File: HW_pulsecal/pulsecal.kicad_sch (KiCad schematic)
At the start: 35 parts, among them J1 BNC_CONN, Q3 FDG6301N, U1 TLV9061IDBVR, U2 TLV9061IDBVR, U5 STM32G030C8Tx

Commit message: update
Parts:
- added C25: 104/50V, Capacitor_SMD:C_0402_1005Metric, symbol Device:C
- added FB1: 600R/100M, Inductor_SMD:L_0603_1608Metric, symbol Device:FerriteBead_Small
- added J4: Conn_01x04, Connector_PinSocket_2.54mm:PinSocket_1x04_P2.54mm_Vertical, symbol Connector_Generic:Conn_01x04
- C20, C21: value 101/50 -> 101/50V
- C7: value 106/6.3V -> 106/16V; footprint Capacitor_SMD:C_0402_1005Metric -> Capacitor_SMD:C_0603_1608Metric
- J1: footprint (none) -> NewLib:BNC_3pin
- R1: footprint Resistor_SMD:R_0402_1005Metric -> Resistor_SMD:R_0603_1608Metric
- R12, R13: value 500M -> 1G
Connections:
- net +3V3: now also FB1.1, J4.1 (Pin_1); no longer U5.5 (VREF+)
- net GND: now also C25.1, J4.3 (Pin_3)
- net HV_ADC: now also U5.12 (PA1); no longer U5.11 (PA0)
- net SWCLK: now also J4.4 (Pin_4)
- net SWDIO: now also J4.2 (Pin_2)
- net dac_fb: now also U5.13 (PA2); no longer U5.12 (PA1)
- net at R10.2, R6.1, U2.1: now also R14.1
- net at R6.2, U2.4 (-): no longer R14.1
- net key_output: now reaches U5.1 (PC13)
- net key_pulse: now reaches U5.2 (PC14)
- net key_add: now reaches U5.3 (PC15)
- net key_sub: now reaches U5.45 (PB6)
- net key_volt: now reaches U5.46 (PB7)
- net key_move: now reaches U5.47 (PB8)
- net key_freq: now reaches U5.48 (PB9)
- new net VAA: C25.2, FB1.2, U5.5 (VREF+)
- new net bat_adc: U5.11 (PA0)
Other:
- note added: "35"
- moved on the sheet: C23, C24, R14

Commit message: update
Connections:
- net DISP_A: now also U5.30 (PC6)
- net DISP_B: now also U5.34 (PA12/PA10)
- net DISP_C: now also U5.23 (PB11)
- net DISP_D: now also U5.21 (PB2)
- net DISP_DIG1: now also U5.27 (PB15)
- net DISP_DIG2: now also U5.22 (PB10)
- net DISP_DIG3: now also U5.32 (PA10/NC)
- net DISP_DIG4: now also U5.38 (PD0)
- net DISP_DIG5: now also U5.40 (PD2)
- net DISP_DIG6: now also U5.44 (PB5)
- net DISP_DP: now also U5.29 (PA9/NC)
- net DISP_E: now also U5.31 (PC7)
- net DISP_F: now also U5.20 (PB1)
- net DISP_G1: now also U5.43 (PB4)
- net DISP_G2: now also U5.41 (PD3)
- net DISP_H: now also U5.26 (PB14)
- net DISP_J: now also U5.24 (PB12)
- net DISP_K: now also U5.42 (PB3)
- net DISP_L: now also U5.39 (PD1)
- net DISP_M: now also U5.37 (PA15)
- net DISP_N: now also U5.33 (PA11/PA9)
- no-connect marks 0 -> 6
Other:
- moved on the sheet: J4

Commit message: update
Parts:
- R1, R15: value 1k -> 1K
- R11: value 2.2k -> 2.2K
- R12, R13: value 1G -> 500M
- R14, R5, R6, R7: value 10k -> 10K
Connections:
- no-connect marks 6 -> 7
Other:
- moved on the sheet: C20, C21, J4, R8, R9

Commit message: Update pulsecal.kicad_sch
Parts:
- R15: value 1K -> NC
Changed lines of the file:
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@@
 			)
 		)
-		(property "Value" "1K"
+		(property "Value" "NC"
 			(at 156.21 73.914 90)
 			(effects

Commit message: update
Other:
- note added: "建议用一颗5~10nF的高压电容代替"
- company: (none) -> 模拟龙仪器仪表
- title: (none) -> 率表/定标器测试工具
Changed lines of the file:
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@@
 	(generator_version "8.0")
 	(paper "A4")
+	(title_block
+		(title "率表/定标器测试工具")
+		(date "2025-06-14")
+		(rev "V1.1")
+		(company "模拟龙仪器仪表")
+	)
 	(junction
 		(at 118.11 116.84)
@@
 	)
 	(rectangle
+		(start 40.64 97.79)
+		(end 63.5 116.84)
+		(stroke
+			(width 0)
+			(type default)
+		)
+		(fill
+			(type none)
+		)
+	)
+	(rectangle
 		(start 91.44 99.06)
 		(end 102.87 106.68)
@@
 		)
 	)
+	(text "建议用一颗5~10nF的高压电容代替"
+		(exclude_from_sim no)
+		(at 52.324 96.52 0)
+		(effects
+			(font
+				(size 1.27 1.27)
+			)
+		)
+	)
 	(text "CH1N\n\nCH1"
 		(exclude_from_sim no)
@@
 	)
 	(sheet
-		(at 180.34 170.18)
-		(size 12.7 8.89)
-		(fields_autoplaced yes)
+		(at 180.34 168.91)
+		(size 12.7 6.35)
 		(stroke
 			(width 0.1524)
@@
 		)
 		(property "Sheetname" "POWER"
-			(at 180.34 169.4684 0)
+			(at 183.388 172.72 0)
 			(effects
 				(font
@@
 		)
 		(property "Sheetfile" "power.kicad_sch"
-			(at 180.34 179.6546 0)
+			(at 180.34 175.8446 0)
 			(effects
 				(font
@@
 	)
 	(sheet
-		(at 195.58 170.18)
-		(size 12.7 8.89)
-		(fields_autoplaced yes)
+		(at 195.58 168.91)
+		(size 12.7 6.35)
 		(stroke
 			(width 0.1524)
@@
 		)
 		(property "Sheetname" "DISP"
-			(at 195.58 169.4684 0)
+			(at 198.628 172.72 0)
 			(effects
 				(font
@@
 		)
 		(property "Sheetfile" "disp.kicad_sch"
-			(at 195.58 179.6546 0)
+			(at 195.58 175.8446 0)
 			(effects
 				(font

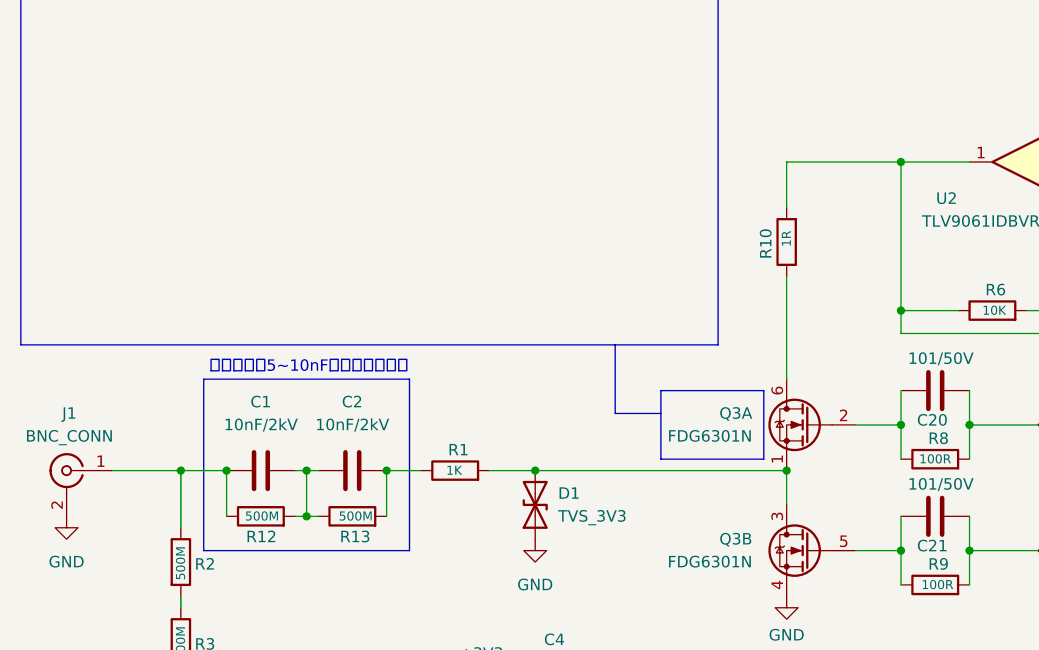
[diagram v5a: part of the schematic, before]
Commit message: 更新
增加了一个电阻，可以极大的减少低压输出的振铃
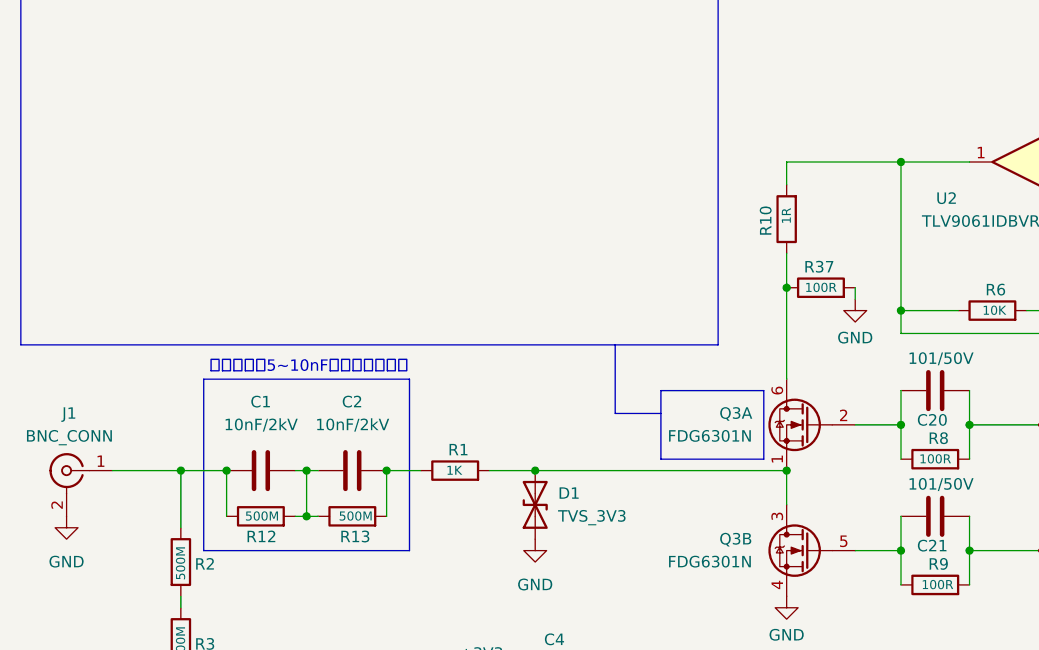
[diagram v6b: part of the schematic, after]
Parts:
- added R37: 100R, Resistor_SMD:R_0402_1005Metric, symbol Device:R
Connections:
- net GND: now also R37.2
- net at Q3.6 (D), R10.1: now also R37.1
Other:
- moved on the sheet: R10
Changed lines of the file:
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@@
 (kicad_sch
-	(version 20231120)
+	(version 20250114)
 	(generator "eeschema")
-	(generator_version "8.0")
+	(generator_version "9.0")
 	(paper "A4")
 	(title_block
@@
 		(company "模拟龙仪器仪表")
 	)
+	(rectangle
+		(start 213.36 16.51)
+		(end 281.94 158.75)
+		(stroke
+			(width 0)
+			(type default)
+		)
+		(fill
+			(type none)
+		)
+	)
+	(rectangle
+		(start 20.32 16.51)
+		(end 97.79 93.98)
+		(stroke
+			(width 0)
+			(type default)
+		)
+		(fill
+			(type none)
+		)
+	)
+	(rectangle
+		(start 40.64 97.79)
+		(end 63.5 116.84)
+		(stroke
+			(width 0)
+			(type default)
+		)
+		(fill
+			(type none)
+		)
+	)
+	(rectangle
+		(start 91.44 99.06)
+		(end 102.87 106.68)
+		(stroke
+			(width 0)
+			(type default)
+		)
+		(fill
+			(type none)
+		)
+	)
+	(text "0.6uA max"
+		(exclude_from_sim no)
+		(at 60.452 136.144 0)
+		(effects
+			(font
+				(size 1.27 1.27)
+			)
+		)
+	)
+	(text "35"
+		(exclude_from_sim no)
+		(at 275.082 154.94 0)
+		(effects
+			(font
+				(size 1.27 1.27)
+			)
+		)
+	)
+	(text "建议用一颗5~10nF的高压电容代替"
+		(exclude_from_sim no)
+		(at 52.324 96.52 0)
+		(effects
+			(font
+				(size 1.27 1.27)
+			)
+		)
+	)
+	(text "CH1N\n\nCH1"
+		(exclude_from_sim no)
+		(at 157.48 40.386 0)
+		(effects
+			(font
+				(size 1.27 1.27)
+				(color 255 255 255 1)
+			)
+		)
+	)
+	(text "1000:1"
+		(exclude_from_sim no)
+		(at 42.672 132.334 0)
+		(effects
+			(font
+				(size 1.27 1.27)
+			)
+		)
+	)
 	(junction
 		(at 118.11 116.84)
@@
 	)
 	(junction
+		(at 105.41 87.63)
+		(diameter 0)
+		(color 0 0 0 0)
+	)
+	(junction
 		(at 38.1 107.95)
 		(diameter 0)
@@
 	(wire
 		(pts
+			(xy 113.03 88.9) (xy 113.03 87.63)
+		)
+		(stroke
+			(width 0)
+			(type default)
+		)
+	)
+	(wire
+		(pts
 			(xy 72.39 107.95) (xy 77.47 107.95)
 		)
@@
 	(wire
 		(pts
+			(xy 105.41 87.63) (xy 105.41 97.79)
+		)
+		(stroke
+			(width 0)
+			(type default)
+		)
+	)
+	(wire
+		(pts
 			(xy 118.11 90.17) (xy 118.11 92.71)
 		)
@@
 	(wire
 		(pts
-			(xy 105.41 86.36) (xy 105.41 97.79)
+			(xy 105.41 83.82) (xy 105.41 87.63)
 		)
 		(stroke
@@
 	(wire
 		(pts
-			(xy 105.41 73.66) (xy 105.41 78.74)
+			(xy 105.41 73.66) (xy 105.41 76.2)
 		)
 		(stroke
@@
 		)
 	)
-	(rectangle
-		(start 213.36 16.51)
-		(end 281.94 158.75)
-		(stroke
-			(width 0)
-			(type default)
-		)
-		(fill
-			(type none)
-		)
-	)
-	(rectangle
-		(start 20.32 16.51)
-		(end 97.79 93.98)
-		(stroke
-			(width 0)
-			(type default)
-		)
-		(fill
-			(type none)
-		)
-	)
-	(rectangle
-		(start 40.64 97.79)
-		(end 63.5 116.84)
-		(stroke
-			(width 0)
-			(type default)
-		)
-		(fill
-			(type none)
-		)
-	)
-	(rectangle
-		(start 91.44 99.06)
-		(end 102.87 106.68)
-		(stroke
-			(width 0)
-			(type default)
-		)
-		(fill
-			(type none)
-		)
-	)
 	(image
 		(at 157.48 34.29)
@@
 		)
 	)
-	(text "0.6uA max"
-		(exclude_from_sim no)
-		(at 60.452 136.144 0)
-		(effects
-			(font
-				(size 1.27 1.27)
-			)
-		)
-	)
-	(text "35"
-		(exclude_from_sim no)
-		(at 275.082 154.94 0)
-		(effects
-			(font
-				(size 1.27 1.27)
-			)
-		)
-	)
-	(text "建议用一颗5~10nF的高压电容代替"
-		(exclude_from_sim no)
-		(at 52.324 96.52 0)
-		(effects
-			(font
-				(size 1.27 1.27)
-			)
-		)
-	)
-	(text "CH1N\n\nCH1"
-		(exclude_from_sim no)
-		(at 157.48 40.386 0)
-		(effects
-			(font
-				(size 1.27 1.27)
-				(color 255 255 255 1)
-			)
-		)
-	)
-	(text "1000:1"
-		(exclude_from_sim no)
-		(at 42.672 132.334 0)
-		(effects
-			(font
-				(size 1.27 1.27)
-			)
-		)
-	)
 	(label "dac"
 		(at 167.64 71.12 0)
-		(fields_autoplaced yes)
 		(effects
 			(font
@@
 	)
 	(symbol
+		(lib_id "Device:R")
+		(at 109.22 87.63 90)
+		(unit 1)
+		(exclude_from_sim no)
+		(in_bom yes)
+		(on_board yes)
+		(dnp no)
+		(property "Reference" "R37"
+			(at 110.744 85.344 90)
+			(effects
+				(font
+					(size 1.27 1.27)
+				)
+				(justify left)
+			)
+		)
+		(property "Value" "100R"
+			(at 110.998 87.63 90)
+			(effects
+				(font
+					(size 1 1)
+				)
+				(justify left)
+			)
+		)
+		(property "Footprint" "Resistor_SMD:R_0402_1005Metric"
+			(at 109.22 89.408 90)
+			(effects
+				(font
+					(size 1.27 1.27)
+				)
+				(hide yes)
+			)
+		)
+		(property "Datasheet" "~"
+			(at 109.22 87.63 0)
+			(effects
+				(font
+					(size 1.27 1.27)
+				)
+				(hide yes)
+			)
+		)
+		(property "Description" "Resistor"
+			(at 109.22 87.63 0)
+			(effects
+				(font
+					(size 1.27 1.27)
+				)
+				(hide yes)
+			)
+		)
+		(pin "2"
+		)
+		(pin "1"
+		)
+		(instances
+			(project "pulsecal"
+				(path "/43467254-5f0e-4dea-8ff8-85167d0157c0"
+					(reference "R37")
+					(unit 1)
+				)
+			)
+		)
+	)
+	(symbol
 		(lib_id "Device:C")
 		(at 76.2 132.08 90)
@@
 	)
 	(symbol
+		(lib_id "power:GND")
+		(at 113.03 88.9 0)
+		(mirror y)
+		(unit 1)
+		(exclude_from_sim no)
+		(in_bom yes)
+		(on_board yes)
+		(dnp no)
+		(property "Reference" "#PWR071"
+			(at 113.03 95.25 0)
+			(effects
+				(font
+					(size 1.27 1.27)
+				)
+				(hide yes)
+			)
+		)
+		(property "Value" "GND"
+			(at 113.03 93.218 0)
+			(effects
+				(font
+					(size 1.27 1.27)
+				)
+			)
+		)
+		(property "Footprint" ""
+			(at 113.03 88.9 0)
+			(effects
+				(font
+					(size 1.27 1.27)
+				)
+				(hide yes)
+			)
+		)
+		(property "Datasheet" ""
+			(at 113.03 88.9 0)
+			(effects
+				(font
+					(size 1.27 1.27)
+				)
+				(hide yes)
+			)
+		)
+		(property "Description" "Power symbol creates a global label with name \"GND\" , ground"
+			(at 113.03 88.9 0)
+			(effects
+				(font
+					(size 1.27 1.27)
+				)
+				(hide yes)
+			)
+		)
+		(pin "1"
+		)
+		(instances
+			(project "pulsecal"
+				(path "/43467254-5f0e-4dea-8ff8-85167d0157c0"
+					(reference "#PWR071")
+					(unit 1)
+				)
+			)
+		)
+	)
+	(symbol
 		(lib_id "Device:R")
 		(at 38.1 127 0)
@@
 	(symbol
 		(lib_id "Device:R")
-		(at 105.41 82.55 180)
+		(at 105.41 80.01 180)
 		(unit 1)
 		(exclude_from_sim no)
@@
 		(dnp no)
 		(property "Reference" "R10"
-			(at 103.124 81.026 90)
+			(at 103.124 78.486 90)
 			(effects
 				(font
@@
 		)
 		(property "Value" "1R"
-			(at 105.41 81.28 90)
+			(at 105.41 78.74 90)
 			(effects
 				(font
@@
 		)
 		(property "Footprint" "Resistor_SMD:R_0402_1005Metric"
-			(at 107.188 82.55 90)
+			(at 107.188 80.01 90)
 			(effects
 				(font
@@
 		)
 		(property "Datasheet" "~"
-			(at 105.41 82.55 0)
+			(at 105.41 80.01 0)
 			(effects
 				(font
@@
 		)
 		(property "Description" "Resistor"
-			(at 105.41 82.55 0)
+			(at 105.41 80.01 0)
 			(effects
 				(font
@@
 		(at 180.34 168.91)
 		(size 12.7 6.35)
+		(exclude_from_sim no)
+		(in_bom yes)
+		(on_board yes)
+		(dnp no)
 		(stroke
 			(width 0.1524)
@@
 		(at 195.58 168.91)
 		(size 12.7 6.35)
+		(exclude_from_sim no)
+		(in_bom yes)
+		(on_board yes)
+		(dnp no)
 		(stroke
 			(width 0.1524)
@@
 		)
 	)
+	(embedded_fonts no)
 )

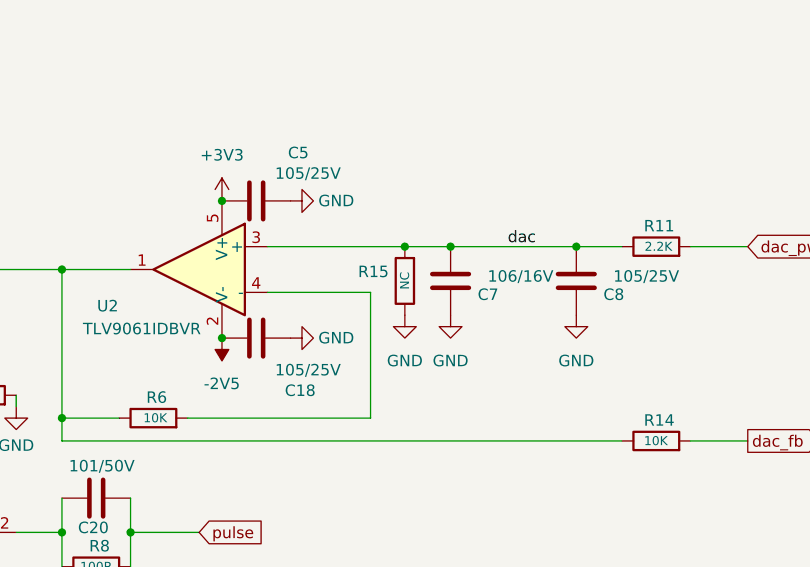
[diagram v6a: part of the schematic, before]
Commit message: update
范围改成2mV-999mV
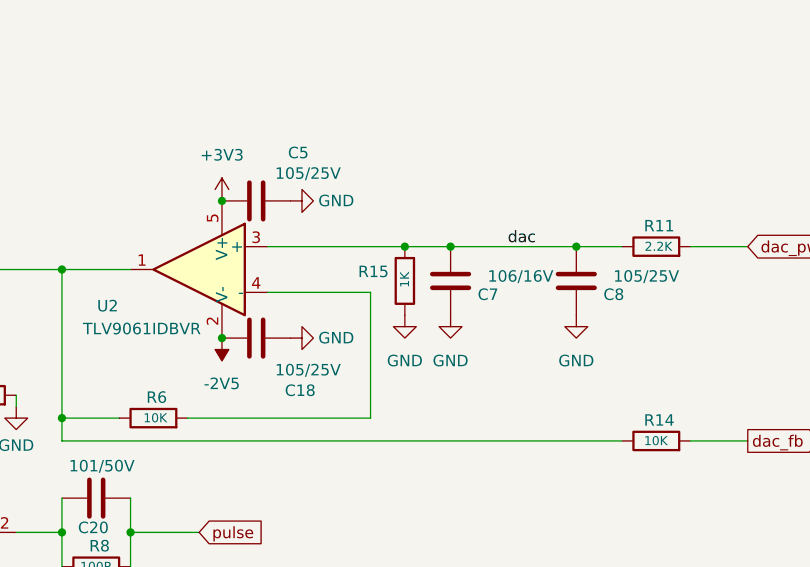
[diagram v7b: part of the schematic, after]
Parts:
- R15: value NC -> 1K
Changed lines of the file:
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@@
 			)
 		)
-		(property "Value" "NC"
+		(property "Value" "1K"
 			(at 156.21 73.914 90)
 			(effects

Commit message: update v1.2
改连接器，改贴片器件为直插器件
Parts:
- removed R12, R13: 500M, Resistor_SMD:R_1206_3216Metric, symbol Device:R
- added C30, C31: 103/50V, Capacitor_SMD:C_0402_1005Metric, symbol Device:C
- C1: value 10nF/2kV -> 10nF/4kV; footprint Capacitor_SMD:C_1206_3216Metric -> Capacitor_THT:C_Rect_L13.5mm_W4.0mm_P10.00mm_FKS3_FKP3_MKS4
- C2: value 10nF/2kV -> NC; footprint Capacitor_SMD:C_1206_3216Metric -> Capacitor_SMD:C_0402_1005Metric
- D1: value TVS_3V3 -> SMBJ3.3CA; footprint Diode_SMD:D_SOD-323_HandSoldering -> Diode_SMD:D_SMB
- J1: footprint NewLib:BNC_3pin -> Connector_Coaxial:BNC_TEConnectivity_1478204_Vertical
- R1: value 1K -> 100R; footprint Resistor_SMD:R_0603_1608Metric -> Resistor_THT:R_Axial_DIN0411_L9.9mm_D3.6mm_P15.24mm_Horizontal
- R14, R7: value 10K -> 100R
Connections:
- net GND: now also C2.2, C30.1, C31.1
- net HV_ADC: now also C30.2
- net dac_fb: now also C31.2
- net at C1.2: now also R1.1; no longer C2.1
- net at Q3.6 (D), R10.1, R37.1: now also C2.1
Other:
- moved on the sheet: C1, R1
